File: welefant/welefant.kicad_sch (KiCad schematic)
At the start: 7 parts, among them J1 Conn_02x11_Odd_Even, J2 Conn_02x11_Odd_Even, Q1 AO3400A, SW1 TS-1187A-B-A-B, SW2 TS-1187A-B-A-B, U1 ESP32-S3-WROOM-1-N8, U2 welefant

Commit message: blubb
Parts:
- removed Q1: AO3400A, easyeda2kicad:SOT-23-3_L2.9-W1.6-P1.90-LS2.8-BR, symbol easyeda2kicad:AO3400A
- removed U1: ESP32-S3-WROOM-1-N8, easyeda2kicad:WIFIM-SMD_ESP32-S3-WROOM-1-N8, symbol easyeda2kicad:ESP32-S3-WROOM-1-N8
- added ANT1: ANTENNA, hacrafu:antenna, symbol hacrafu:antenna
- added BT1: Battery, hacrafu:LiPo_Recycled_welefant, symbol Device:Battery_Cell
- added C1, C2: 33n, easyeda2kicad:C0603, symbol easyeda2kicad:CL10B333KB8NNNC
- added C10, C11: 15p, easyeda2kicad:C0603, symbol easyeda2kicad:CL10C150JB8NNNC
- added C12, C3, C4, C5, C7, C8, C9: 10u, easyeda2kicad:C0603, symbol easyeda2kicad:CL10A106KP8NNNC
- added C13, C14, C22, C25, C6: 1u, easyeda2kicad:C0603, symbol easyeda2kicad:CL10A105KB8NNNC
- added C15, C16, C17, C20, C21, C23, C24: 100n, easyeda2kicad:C0603, symbol easyeda2kicad:CC0603KRX7R9BB104
- added C18: 4p7, easyeda2kicad:C0402, symbol easyeda2kicad:0402CG4R7C500NT
- added C19: 3p3, easyeda2kicad:C0402, symbol easyeda2kicad:0402CG3R3C500NT
- added CLED1: yellow, easyeda2kicad:LED0603-RD-YELLOW, symbol easyeda2kicad:19-213_Y2C-CQ2R2L_3T(CY)
- added D1, D2: 3V3, easyeda2kicad:LL-34_L3.5-W1.5-RD, symbol easyeda2kicad:ZMM3V3
- added D3: 5V6, easyeda2kicad:LL-34_L3.5-W1.5-RD, symbol easyeda2kicad:ZMM5V6
- added D4: 1N5819WS, Diode_SMD:D_SOD-323, symbol Diode:1N5819WS
- added J1: Conn_01x02, Connector_JST:JST_PH_B2B-PH-K_1x02_P2.00mm_Vertical, symbol Connector_Generic:Conn_01x02
- added L1, L2: 2n2, easyeda2kicad:L0603, symbol easyeda2kicad:SDCL1608C2N2STDF
- added LED1, LED10, LED11, LED12, LED13, LED14, LED15, LED16, LED17, LED18, LED19, LED2, LED20, LED3, LED4, LED5, LED6, LED7, LED8, LED9, LEDH_R1: SK6812MINI-E, hacrafu:SK6812MINI-E-handsolder, symbol hacrafu:SK6812MINI-E
- added LED21: blue, easyeda2kicad:LED0603-FD_BLUE, symbol hacrafu:led_fixed
- added LEDH_L1: SK6812MINI-E, hacrafu:SK6812MINI-E-handsolder, symbol easyeda2kicad:SK6812MINI-E_C5149201
- added Q1, Q2, Q3: AO3401A, easyeda2kicad:SOT-23_L2.9-W1.3-P1.90-LS2.4-BR, symbol easyeda2kicad:AO3401A
- added R1, R11, R13, R19: 10K, easyeda2kicad:R0603, symbol easyeda2kicad:0603WAF1002T5E
- added R10, R14, R3: 1K, easyeda2kicad:R0603, symbol easyeda2kicad:0603WAF1001T5E
- added R12, R20: 330, easyeda2kicad:R0603, symbol easyeda2kicad:0603WAF3300T5E
- added R15: 390K, easyeda2kicad:R0603, symbol easyeda2kicad:0603WAF3903T5E
- added R16, R9: 100K, easyeda2kicad:R0603, symbol easyeda2kicad:0603WAF1003T5E
- added R17: 3K3, easyeda2kicad:R0603_NEW, symbol easyeda2kicad:0603WAF3301T5E
- added R18, R21, R22, R23, R24, R25: 0, easyeda2kicad:R0603, symbol easyeda2kicad:0603WAF0000T5E
- added R2, R8: 5.1K, easyeda2kicad:R0603, symbol easyeda2kicad:0603WAF5101T5E
- added R4, R5: 270, easyeda2kicad:R0603, symbol easyeda2kicad:0603WAF2700T5E
- added R6, R7: 150, easyeda2kicad:R0603, symbol easyeda2kicad:0603WAF1500T5E
- added SW1: ON-OFF, easyeda2kicad:SW-TH_K3-1296S-E1, symbol easyeda2kicad:K3-1296S-E1_C128955
- added SW4: GPIO33, easyeda2kicad:SW-SMD_4P-L5.1-W5.1-P3.70-LS6.5-TL-2, symbol easyeda2kicad:TS-1187A-B-A-B
- added SW5: IO34, easyeda2kicad:SW-SMD_4P-L5.1-W5.1-P3.70-LS6.5-TL-2, symbol easyeda2kicad:TS-1187A-B-A-B
- added U1: RT9080-33GJ5, easyeda2kicad:TSOT-23-5_L2.9-W1.6-P0.95-LS2.8-BL, symbol easyeda2kicad:RT9080-33GJ5
- added U2: Audio Jack PJ-324, easyeda2kicad:AUDIO-TH_PJ-32400, symbol easyeda2kicad:PJ-32400
- added U3: SD18OB261-060, hacrafu:MIC-SMD_SD18OB261-060, symbol easyeda2kicad:SD18OB261-060
- added U4: TP4056, easyeda2kicad:ESOP-8_L4.9-W3.9-P1.27-LS6.0-BL-EP, symbol easyeda2kicad:TP4056
- added U6: 128MBit Flash, easyeda2kicad:SOIC-8_L5.3-W5.3-P1.27-LS8.0-BL, symbol easyeda2kicad:W25Q128JVSIQTR
- added U7: ESP32-S3, easyeda2kicad:QFN-56_L7.0-W7.0-P0.40-TL-EP4.0, symbol easyeda2kicad:ESP32-S3
- added U8: Reset 2.8V, easyeda2kicad:SOT-23-3_L2.9-W1.6-P1.90-LS2.8-BR, symbol easyeda2kicad:VDD281MNTA
- added USB1: USB-TYPE-C-018, easyeda2kicad:USB-C_SMD-TYPE-C-31-M-12, symbol easyeda2kicad:USB-TYPE-C-018
- added X1: 40 MHz, easyeda2kicad:OSC-SMD_4P-L3.2-W2.5-BL_SIT8008BI, symbol easyeda2kicad:X322540MPB4SI
- J2: renamed from J1; value Conn_02x11_Odd_Even -> Conn_02x7_Odd_Even; footprint Connector_PinHeader_2.54mm:PinHeader_2x11_P2.54mm_Vertical_SMD -> hacrafu:PinHeader_2x07_P2.54mm_Vertical_SMD_handsolder; symbol Connector_Generic:Conn_02x11_Odd_Even -> Connector_Generic:Conn_02x07_Odd_Even
- J3: renamed from J2; value Conn_02x11_Odd_Even -> Conn_02x6_Odd_Even; footprint Connector_PinHeader_2.54mm:PinHeader_2x11_P2.54mm_Vertical_SMD -> hacrafu:PinHeader_2x06_P2.54mm_Vertical_SMD_handsolder; symbol Connector_Generic:Conn_02x11_Odd_Even -> Connector_Generic:Conn_02x06_Odd_Even
- SW2: renamed from SW1; value TS-1187A-B-A-B -> RESET
- SW3: renamed from SW2; value TS-1187A-B-A-B -> BOOT
- renumbered U2 to U5
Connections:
- net EN is gone; now on net RESET: SW2.1 (A)
- net GND: now also J2.1 (Pin_1), J3.2 (Pin_2), J3.4 (Pin_4), SW2.4 (D), SW3.4 (D), ANT1.GND, BT1.2 (-), C1.1, C10.2, C11.1, C12.2, C13.1, C14.2, C15.1, C16.2, C17.1, C18.1, C19.1, C2.1, C20.1, C21.1, C22.2, C23.1, C24.2, C25.2, C3.1, C6.1, C7.2, C8.1, C9.1, D1.2 (A), D2.2 (A), D3.2 (A), J1.2 (Pin_2), LED1.3 (GND), LED10.3 (GND), LED11.3 (GND), LED12.3 (GND), LED13.3 (GND), LED14.3 (GND), LED15.3 (GND), LED16.3 (GND), LED17.3 (GND), LED18.3 (GND), LED19.3 (GND), LED2.3 (GND), LED20.3 (GND), LED3.3 (GND), LED4.3 (GND), LED5.3 (GND), LED6.3 (GND), LED7.3 (GND), LED8.3 (GND), LED9.3 (GND), LEDH_L1.3 (GND), LEDH_R1.3 (GND), R11.1, R16.2, R17.2, R2.1, R20.1, R6.1, R7.1, R8.2, SW4.3 (C), SW4.4 (D), SW5.3 (C), SW5.4 (D), U1.2 (GND), U2.1, U3.2 (L/R), U3.3 (GND), U4.1 (TEMP), U4.3 (GND), U4.9 (EP), U6.4 (GND), U7.57 (EP), U8.2 (VSS), USB1.A1 (GND), USB1.A12 (GND), USB1.B1 (GND), USB1.B12 (GND), X1.2 (GND), X1.4 (GND)
- net IO0: now also SW3.2 (B), U7.5 (GPIO0)
- net VEXT: now also J3.1 (Pin_1), C24.1, C25.1, LED1.1 (VDD), LED10.1 (VDD), LED11.1 (VDD), LED12.1 (VDD), LED13.1 (VDD), LED14.1 (VDD), LED15.1 (VDD), LED16.1 (VDD), LED17.1 (VDD), LED18.1 (VDD), LED19.1 (VDD), LED2.1 (VDD), LED20.1 (VDD), LED3.1 (VDD), LED4.1 (VDD), LED5.1 (VDD), LED6.1 (VDD), LED7.1 (VDD), LED8.1 (VDD), LED9.1 (VDD), LEDH_L1.1 (VDD), LEDH_R1.1 (VDD), Q1.3 (D), U3.5 (VDD)
- net VEXT_EN: now also J3.3 (Pin_3), R1.2, R3.2, U7.17 (GPIO12)
- net IO40: now reaches J3.10 (Pin_10)
- net IO40: now also U7.45 (MTDO)
- net IO41: now reaches J3.11 (Pin_11)
- net IO41: now also U7.47 (MTDI)
- net IO42: now reaches J3.12 (Pin_12)
- net IO42: now also U7.48 (MTMS)
- net IO35: now reaches J3.5 (Pin_5)
- net IO35: now also U7.40 (GPIO35)
- net IO36: now reaches J3.6 (Pin_6)
- net IO36: now also U7.41 (GPIO36)
- net IO37: now reaches J3.7 (Pin_7)
- net IO37: now also U7.42 (GPIO37)
- net IO38: now reaches J3.8 (Pin_8)
- net IO38: now also U7.43 (GPIO38)
- net IO39: now reaches J3.9 (Pin_9)
- net IO39: now also U7.44 (MTCK)
- net TOUCH_EL: now reaches U5.1 (EarL)
- net TOUCH_EL: now also U7.6 (GPIO1)
- net TOUCH_ER: now reaches U5.2 (EarR)
- net TOUCH_ER: now also U7.7 (GPIO2)
- net TOUCH_T1: now reaches U5.3 (Toe1)
- net TOUCH_T1: now also U7.9 (GPIO4)
- net TOUCH_T2: now reaches U5.4 (Toe2)
- net TOUCH_T2: now also U7.10 (GPIO5)
- net TOUCH_T3: now reaches U5.5 (Toe3)
- net TOUCH_T3: now also U7.11 (GPIO6)
- net TOUCH_T4: now reaches U5.6 (Toe4)
- net TOUCH_T4: now also U7.12 (GPIO7)
- net TOUCH_T5: now reaches U5.7 (Toe5)
- net TOUCH_T5: now also U7.13 (GPIO8)
- net TOUCH_T6: now reaches U5.8 (Toe6)
- net TOUCH_T6: now also U7.14 (GPIO9)
- net MIC_CLK: now reaches J2.10 (Pin_10)
- net MIC_CLK: now also U3.4 (CLK), U7.18 (GPIO13)
- net AUDIO_PWM_R: now reaches J2.11 (Pin_11)
- net AUDIO_PWM_R: now also R5.1, U7.24 (GPIO18)
- net AUDIO_PWM_L: now reaches J2.12 (Pin_12)
- net AUDIO_PWM_L: now also R4.1, U7.23 (GPIO17)
- net USB_DP: now reaches J2.13 (Pin_13)
- net USB_DP: now also D1.1 (C), U7.26 (GPIO20), USB1.A6 (DP1), USB1.B6 (DP2)
- net USB_DN: now reaches J2.14 (Pin_14)
- net USB_DN: now also D2.1 (C), U7.25 (GPIO19), USB1.A7 (DN1), USB1.B7 (DN2)
- net V33: now reaches J2.2 (Pin_2)
- net V33: now also C12.1, C13.2, C15.2, C16.1, C21.2, C23.2, C3.2, L1.1, Q1.2 (S), R1.1, R13.1, R19.1, U1.5 (VOUT), U7.20 (VDD3P3_RTC), U7.46 (VDD3P3_CPU), U7.55 (VDDA), U7.56 (VDDA), U8.3 (VIN)
- net RX: now reaches J2.3 (Pin_3)
- net RX: now also U7.50 (U0RXD)
- net V5: now reaches J2.4 (Pin_4)
- net V5: now also C7.1, CLED1.2 (A), D3.1 (C), D4.2 (A), R10.2, R11.2, U4.4 (VCC), U4.8 (CE), USB1.A4 (VBUS), USB1.A9 (VBUS), USB1.B4 (VBUS), USB1.B9 (VBUS)
- net TX: now reaches J2.5 (Pin_5)
- net TX: now also U7.49 (U0TXD)
- net BAT_SENS: now reaches J2.6 (Pin_6)
- net BAT_SENS: now also C8.2, R15.1, R16.1, U7.15 (GPIO10)
- net BAT_SENS_EN: now reaches J2.7 (Pin_7)
- net BAT_SENS_EN: now also R13.2, R14.2, U7.16 (GPIO11)
- net MIC_DATA: now reaches J2.8 (Pin_8)
- net MIC_DATA: now also U3.1 (Data), U7.19 (GPIO14)
- net JACK_SENS: now reaches J2.9 (Pin_9)
- net JACK_SENS: now also U2.3, U7.22 (XTAL_32K_N)
- net RESET: now reaches SW2.2 (B)
- net RESET: now also C14.1, R19.2, U7.4 (CHIP_PU), U8.1 (VOUT)
- new net: LED7.2 (DOUT), LED8.4 (DIN)
- new net: R9.1, U1.3 (EN)
- new net: R17.1, U4.2 (PROG)
- new net: C1.2, C4.1, R4.2, R6.2
- new net: R2.2, USB1.B5 (CC2)
- new net: LED6.2 (DOUT), LED7.4 (DIN)
- new net: LED5.2 (DOUT), LED6.4 (DIN)
- new net: LEDH_L1.2 (DOUT), LEDH_R1.4 (DIN)
- new net: LED3.2 (DOUT), LED4.4 (DIN)
- new net: Q3.1 (G), R14.1
- new net: Q3.3 (D), R15.2
- new net: LED15.2 (DOUT), LED16.4 (DIN)
- new net: LED14.2 (DOUT), LED15.4 (DIN)
- new net: C11.2, R18.2, X1.3 (OSC2)
- new net: LED10.2 (DOUT), LED11.4 (DIN)
- new net: LED10.4 (DIN), LED9.2 (DOUT)
- new net: LED19.2 (DOUT), LED20.4 (DIN)
- new net: LED18.2 (DOUT), LED19.4 (DIN)
- new net: R23.1, U7.33 (SPICLK)
- new net: C17.2, L1.2, U7.2 (VDD3P3), U7.3 (VDD3P3)
- new net: Q2.1 (G), R10.1
- new net: D4.1 (K), Q2.2 (S), SW1.2
- new net: C18.2, L2.1, U7.1 (LNA_IN)
- new net: R25.1, U7.30 (SPIHD)
- new net: R24.1, U7.31 (SPIWP)
- new net: R22.1, U7.34 (SPIQ)
- new net: R21.1, U7.35 (SPID)
- new net: LED17.2 (DOUT), LED18.4 (DIN)
- new net: LED1.2 (DOUT), LED2.4 (DIN)
- new net: C2.2, C5.1, R5.2, R7.2
- new net: CLED1.1 (C), R12.1
- new net: R12.2, U4.7 (~{CHRG})
- new net: C5.2, U2.2
- new net: C4.2, U2.5
- new net: LED2.2 (DOUT), LED3.4 (DIN)
- new net: ANT1.FEED, C19.2, L2.2
- new net: LED21.1 (C), R20.2
- new net: R8.1, USB1.A5 (CC1)
- new net: LED13.2 (DOUT), LED14.4 (DIN)
- new net: Q1.1 (G), R3.1
- new net: LED11.2 (DOUT), LED12.4 (DIN)
- new net D1_LED: LED4.2 (DOUT), LED5.4 (DIN)
- new net D2_LED: LED8.2 (DOUT), LED9.4 (DIN)
- new net D3_LED: LED12.2 (DOUT), LED13.4 (DIN)
- new net D4_LED: LED16.2 (DOUT), LED17.4 (DIN)
- new net GPIO33: SW4.1 (A), SW4.2 (B), U7.38 (GPIO33)
- new net GPIO34: SW5.1 (A), SW5.2 (B), U7.39 (GPIO34)
- new net LED: LED21.2 (A), U7.21 (XTAL_32K_P)
- new net LED_HEAD: LEDH_L1.4 (DIN), U7.37 (SPICLK_P)
- new net LED_MATRIX: LED1.4 (DIN), U7.36 (SPICLK_N)
- new net SPICLK: R23.2, U6.6 (CLK)
- new net SPICS0: U6.1 (~{CS}), U7.32 (SPICS0)
- new net SPID: R21.2, U6.5 (DI)
- new net SPIHD: R25.2, U6.7 (IO3)
- new net SPIQ: R22.2, U6.2 (DO)
- new net SPIWP: R24.2, U6.3 (IO2)
- new net VBAT: BT1.1 (+), C9.2, J1.1 (Pin_1), Q2.3 (D), Q3.2 (S), U4.5 (BAT)
- new net VBUS: C6.2, R9.2, SW1.3, U1.1 (VIN)
- new net VDD_SPI: C20.2, C22.1, U6.8 (VCC), U7.29 (VDD_SPI)
- new net XTAL_N: C10.1, U7.53 (XTAL_N), X1.1 (OSC1)
- new net XTAL_P: R18.1, U7.54 (XTAL_P)
- no-connect marks 0 -> 21
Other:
- removed sheet LEDs
- removed sheet Microphone and Speaker
- removed sheet Power
- note added: "3.3V & VEXT"
- note added: "Audio Jack & Mic"
- note added: "Battery Charging"
- note added: "Battery Sensing"
- note added: "Connectors"
- note added: "ESP32-S3"
- note added: "RGB LEDs"
- note added: "USB-C"
- title: (none) -> Welefant
- moved on the sheet: SW2, SW3

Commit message: welefant bestellung
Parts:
- BT2: renamed from J1; footprint Connector_JST:JST_PH_B2B-PH-K_1x02_P2.00mm_Vertical -> Connector_JST:JST_XH_B2B-XH-A_1x02_P2.50mm_Vertical
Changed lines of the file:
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@@
   (symbol (lib_id "Connector_Generic:Conn_01x02") (at 177.8 62.865 0) (unit 1)
     (in_bom yes) (on_board yes) (dnp no)
-    (property "Reference" "J1" (at 177.8 68.58 0)
+    (property "Reference" "BT2" (at 177.8 68.58 0)
       (effects (font (size 1.27 1.27)))
     )
@@
       (effects (font (size 1.27 1.27)) hide)
     )
-    (property "Footprint" "Connector_JST:JST_PH_B2B-PH-K_1x02_P2.00mm_Vertical" (at 177.8 62.865 0)
+    (property "Footprint" "Connector_JST:JST_XH_B2B-XH-A_1x02_P2.50mm_Vertical" (at 177.8 62.865 0)
       (effects (font (size 1.27 1.27)) hide)
     )
@@
       (project "welefant"
         (path "/97f5bd5b-f387-4518-b83a-fa60b8a606f1"
-          (reference "J1") (unit 1)
+          (reference "BT2") (unit 1)
         )
       )

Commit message: stand
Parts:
- removed C17, C20: 100n, easyeda2kicad:C0603, symbol easyeda2kicad:CC0603KRX7R9BB104
- removed C18: 4p7, easyeda2kicad:C0402, symbol easyeda2kicad:0402CG4R7C500NT
- removed C19: 3p3, easyeda2kicad:C0402, symbol easyeda2kicad:0402CG3R3C500NT
- removed C22: 1u, easyeda2kicad:C0603, symbol easyeda2kicad:CL10A105KB8NNNC
- removed R21, R22, R23, R24, R25: 0, easyeda2kicad:R0603, symbol easyeda2kicad:0603WAF0000T5E
- removed U6: 128MBit Flash, easyeda2kicad:SOIC-8_L5.3-W5.3-P1.27-LS8.0-BL, symbol easyeda2kicad:W25Q128JVSIQTR
- added C17: 100n, easyeda2kicad:C0402_NEW, symbol easyeda2kicad:CL05B104KO5NNNC
- added C18, C19: 3p3, easyeda2kicad:C0603, symbol easyeda2kicad:0603CG3R3C500NT
- J2: value Conn_02x7_Odd_Even -> Conn_02x6_Odd_Even; footprint hacrafu:PinHeader_2x07_P2.54mm_Vertical_SMD_handsolder -> hacrafu:PinHeader_2x06_P2.54mm_Vertical_SMD_handsolder; symbol Connector_Generic:Conn_02x07_Odd_Even -> Connector_Generic:Conn_02x06_Odd_Even
- J3: value Conn_02x6_Odd_Even -> Conn_02x7_Odd_Even; footprint hacrafu:PinHeader_2x06_P2.54mm_Vertical_SMD_handsolder -> hacrafu:PinHeader_2x07_P2.54mm_Vertical_SMD_handsolder; symbol Connector_Generic:Conn_02x06_Odd_Even -> Connector_Generic:Conn_02x07_Odd_Even
- U7: value ESP32-S3 -> ESP32-S3(FN8); LCSC Part C2913192 -> C2913196
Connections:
- net AUDIO_PWM_L: now also J2.10 (Pin_10); no longer J2.12 (Pin_12)
- net AUDIO_PWM_R: now also J2.9 (Pin_9); no longer J2.11 (Pin_11)
- net BAT_SENS: now also J2.4 (Pin_4); no longer J2.6 (Pin_6)
- net BAT_SENS_EN: now also J2.5 (Pin_5); no longer J2.7 (Pin_7)
- net GND: now also ANT1.2 (GND), C17.1, C18.1, C19.1; no longer ANT1.GND
- net IO35: now also J3.7 (Pin_7); no longer J3.5 (Pin_5)
- net IO36: now also J3.8 (Pin_8); no longer J3.6 (Pin_6)
- net IO37: now also J3.9 (Pin_9); no longer J3.7 (Pin_7)
- net IO38: now also J3.10 (Pin_10); no longer J3.8 (Pin_8)
- net IO39: now also J3.11 (Pin_11); no longer J3.9 (Pin_9)
- net IO40: now also J3.12 (Pin_12); no longer J3.10 (Pin_10)
- net IO41: now also J3.13 (Pin_13); no longer J3.11 (Pin_11)
- net IO42: now also J3.14 (Pin_14); no longer J3.12 (Pin_12)
- net JACK_SENS: now also J2.7 (Pin_7); no longer J2.9 (Pin_9)
- net MIC_CLK: now also J2.6 (Pin_6); no longer J2.10 (Pin_10)
- net RX: now also J3.5 (Pin_5); no longer J2.3 (Pin_3)
- net TX: now also J3.6 (Pin_6); no longer J2.5 (Pin_5)
- net USB_DN: now also J2.12 (Pin_12); no longer J2.14 (Pin_14)
- net USB_DP: now also J2.11 (Pin_11); no longer J2.13 (Pin_13)
- net V5: now also J2.3 (Pin_3); no longer J2.4 (Pin_4)
- net at L1.2, U7.2 (VDD3P3), U7.3 (VDD3P3): now also C17.2
- net at L2.1, U7.1 (LNA_IN): now also C19.2
- net at L2.2: now also ANT1.1 (FEED), C18.2; no longer ANT1.FEED
- net SPICS0: no longer names the net of U7.32 (SPICS0)
- net VDD_SPI: no longer names the net of U7.29 (VDD_SPI)
- no-connect marks 21 -> 28

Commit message: welefant redesign
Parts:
- removed C18, C19: 3p3, easyeda2kicad:C0603, symbol easyeda2kicad:0603CG3R3C500NT
- removed D1, D2: 3V3, easyeda2kicad:LL-34_L3.5-W1.5-RD, symbol easyeda2kicad:ZMM3V3
- removed D3: 5V6, easyeda2kicad:LL-34_L3.5-W1.5-RD, symbol easyeda2kicad:ZMM5V6
- removed LED21: blue, easyeda2kicad:LED0603-FD_BLUE, symbol hacrafu:led_fixed
- added C18, C19: 3p3, easyeda2kicad:C0603, symbol easyeda2kicad:GRM1885C1H3R3BA01D
- added D1, D2, D3: 5V6, easyeda2kicad:SOD-523_L1.2-W0.8-LS1.6-BI, symbol easyeda2kicad:LESD5D5.0CT1G
- added LED21: white, easyeda2kicad:LED0603-R-RD_WHITE, symbol easyeda2kicad:0603Whitelight_C2290
- ANT1: now left out of the parts list
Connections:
- net GND: now also C18.1, C19.1, D1.2, D2.2, D3.2
- net LED: now also LED21.1 (A)
- net USB_DN: now also D2.1
- net USB_DP: now also D1.1
- net V5: now also D3.1
- net at L2.1, U7.1 (LNA_IN): now also C19.2
- net at R20.2: now also LED21.2 (K)
- net at ANT1.1 (FEED), L2.2: now also C18.2
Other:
- moved on the sheet: L2

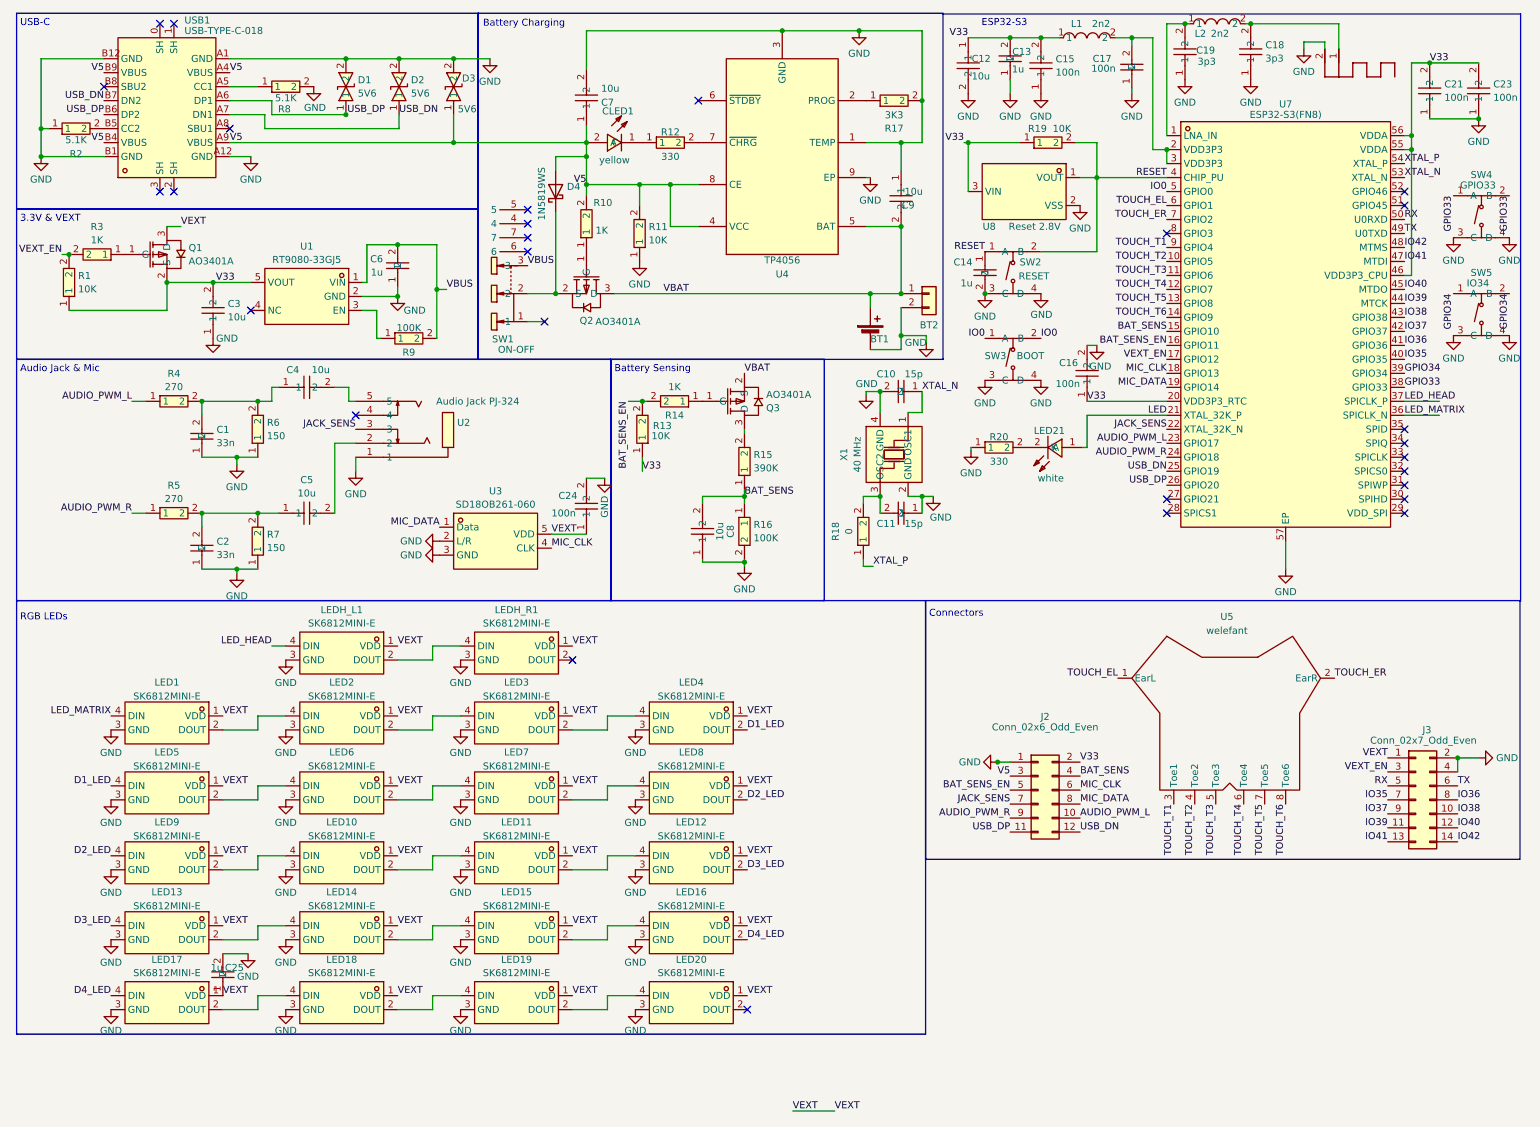
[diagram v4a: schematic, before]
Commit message: welefant: add fuse and make LED cutout smaller
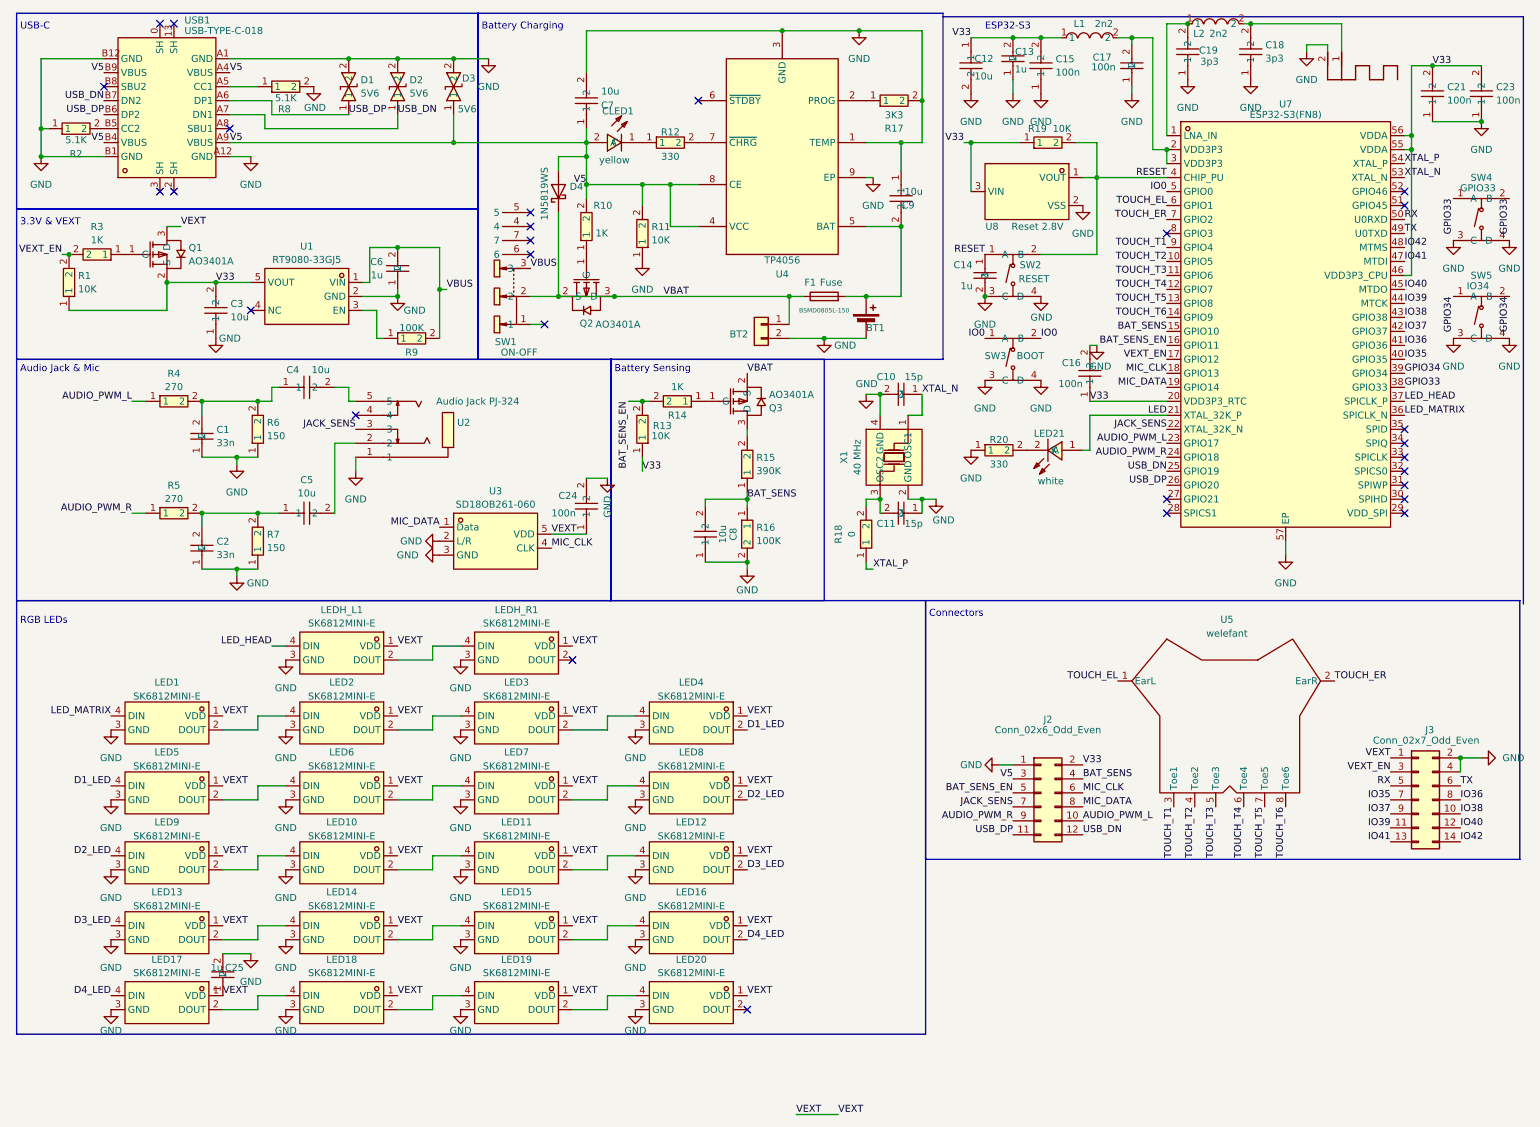
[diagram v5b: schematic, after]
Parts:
- added F1: Fuse, easyeda2kicad:F0805, symbol Device:Fuse
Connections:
- net VBAT: now also D4.1 (K), Q2.2 (S), SW1.2, F1.1; no longer BT1.1 (+), C9.2, U4.5 (BAT)
- new net: BT1.1 (+), C9.2, F1.2, U4.5 (BAT)
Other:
- moved on the sheet: BT1, BT2, C10, C12, C13, C14, C16, C19, C21, C23, C3, C6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

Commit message: stand bestellung 18.5.25
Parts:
- removed C14: 1u, easyeda2kicad:C0603, symbol easyeda2kicad:CL10A105KB8NNNC
- removed CLED1: yellow, easyeda2kicad:LED0603-RD-YELLOW, symbol easyeda2kicad:19-213_Y2C-CQ2R2L_3T(CY)
- removed D1, D2, D3: 5V6, easyeda2kicad:SOD-523_L1.2-W0.8-LS1.6-BI, symbol easyeda2kicad:LESD5D5.0CT1G
- removed R19: 10K, easyeda2kicad:R0603, symbol easyeda2kicad:0603WAF1002T5E
- removed U8: Reset 2.8V, easyeda2kicad:SOT-23-3_L2.9-W1.6-P1.90-LS2.8-BR, symbol easyeda2kicad:VDD281MNTA
- added CLED1: yellow, easyeda2kicad:LED0805-R-RD, symbol easyeda2kicad:17-21SUYC_TR8
- added D1, D2, D3: 5V6, easyeda2kicad:SOD-882_L1.0-W0.6-BI, symbol easyeda2kicad:H5VL10B
- added U6: Reset 2V9, easyeda2kicad:SOT-143_L2.9-W1.3-P1.92-LS2.3-BR, symbol easyeda2kicad:IMP811S-TD
- D4: LCSC Part (none) -> C191023
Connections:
- net GND: now also D1.2 (A), D2.2 (A), D3.2 (A), U6.1 (GND)
- net GPIO33: now also J2.11 (Pin_11)
- net RESET: now also U6.4 (~{MR}); no longer U7.4 (CHIP_PU)
- net USB_DN: now also D2.1 (C); no longer J2.12 (Pin_12)
- net USB_DP: now also D1.1 (C); no longer J2.11 (Pin_11)
- net V33: now also U6.3 (VCC)
- net V5: now also CLED1.1 (+), D3.1 (C)
- net VBAT: now also C9.2, J2.12 (Pin_12), U4.5 (BAT); no longer BT2.1 (Pin_1), D4.1 (K), Q2.2 (S), SW1.2
- net at BT1.1 (+), F1.2: now also BT2.1 (Pin_1); no longer C9.2, U4.5 (BAT)
- net at R12.1: now also CLED1.2 (-)
- new net: D4.1 (K), Q2.2 (S), SW1.2
- new net: U6.2 (~{RESET}), U7.4 (CHIP_PU)
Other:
- moved on the sheet: BT1, BT2, F1, SW2
